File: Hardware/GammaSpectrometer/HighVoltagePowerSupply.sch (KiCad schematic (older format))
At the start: 59 parts, among them J1 power supply, J2 anode, J3 cathode, J4 Conn_01x07_Female, J5 RF_Shield_Two_Pieces, Q1 AOD2810, U1 MCP1416

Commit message: HV Power Supply and DataAcquisition will be placed on the same PCB. Due to EMI it mightl be needed to mount them on separate PCB, still they will share the same layout. This will decrease amount of needed PCBs and reduce costs.
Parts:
- J1: footprint HighVoltagePowerSupply:DG300-5.0-02P-12-00A(H) -> GammaSpectrometer:DG300-5.0-02P-12-00A(H)
- J5: footprint HighVoltagePowerSupply:3710.16 -> GammaSpectrometer:3710.16
- TR1: footprint HighVoltagePowerSupply:RM8 -> GammaSpectrometer:RM8; symbol HighVoltagePowerSupply:RM8 -> GammaSpectrometer:RM8

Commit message: Applied some remarks after second hw review (#104). Basically only removed voltage divider and replaced it by additional transformer winding.
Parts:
- removed C15: 1n, Capacitor_SMD:C_1206_3216Metric, symbol Device:C
- removed D3: 5V, Diode_SMD:D_SMA, symbol Device:D_Zener
- removed R10: 5k6, Resistor_SMD:R_MELF_MMB-0207, symbol Device:R
- removed R11, R12, R13, R14, R15, R7, R8, R9: 10M, Resistor_SMD:R_MELF_MMB-0207, symbol Device:R
- removed R16, R17: 47k, Resistor_SMD:R_MELF_MMB-0207, symbol Device:R
- added C15: 10u/12V, Capacitor_SMD:CP_Elec_10x10, symbol Device:CP
- added C17: 100n, Capacitor_SMD:C_1206_3216Metric, symbol Device:C
- added D3: D, symbol Device:D
- added L3: TBD, symbol Device:L_Core_Ferrite
- R5, R6: value 10M -> 6k8; footprint Resistor_SMD:R_MELF_MMB-0207 -> Resistor_SMD:R_1206_3216Metric
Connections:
- net labels removed: V_DIVIDER
- wire segments 178 -> 168
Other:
- moved on the sheet: C11, C12, C13, C14, C6, C8, D2, J2, J3, L2, R18, R4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

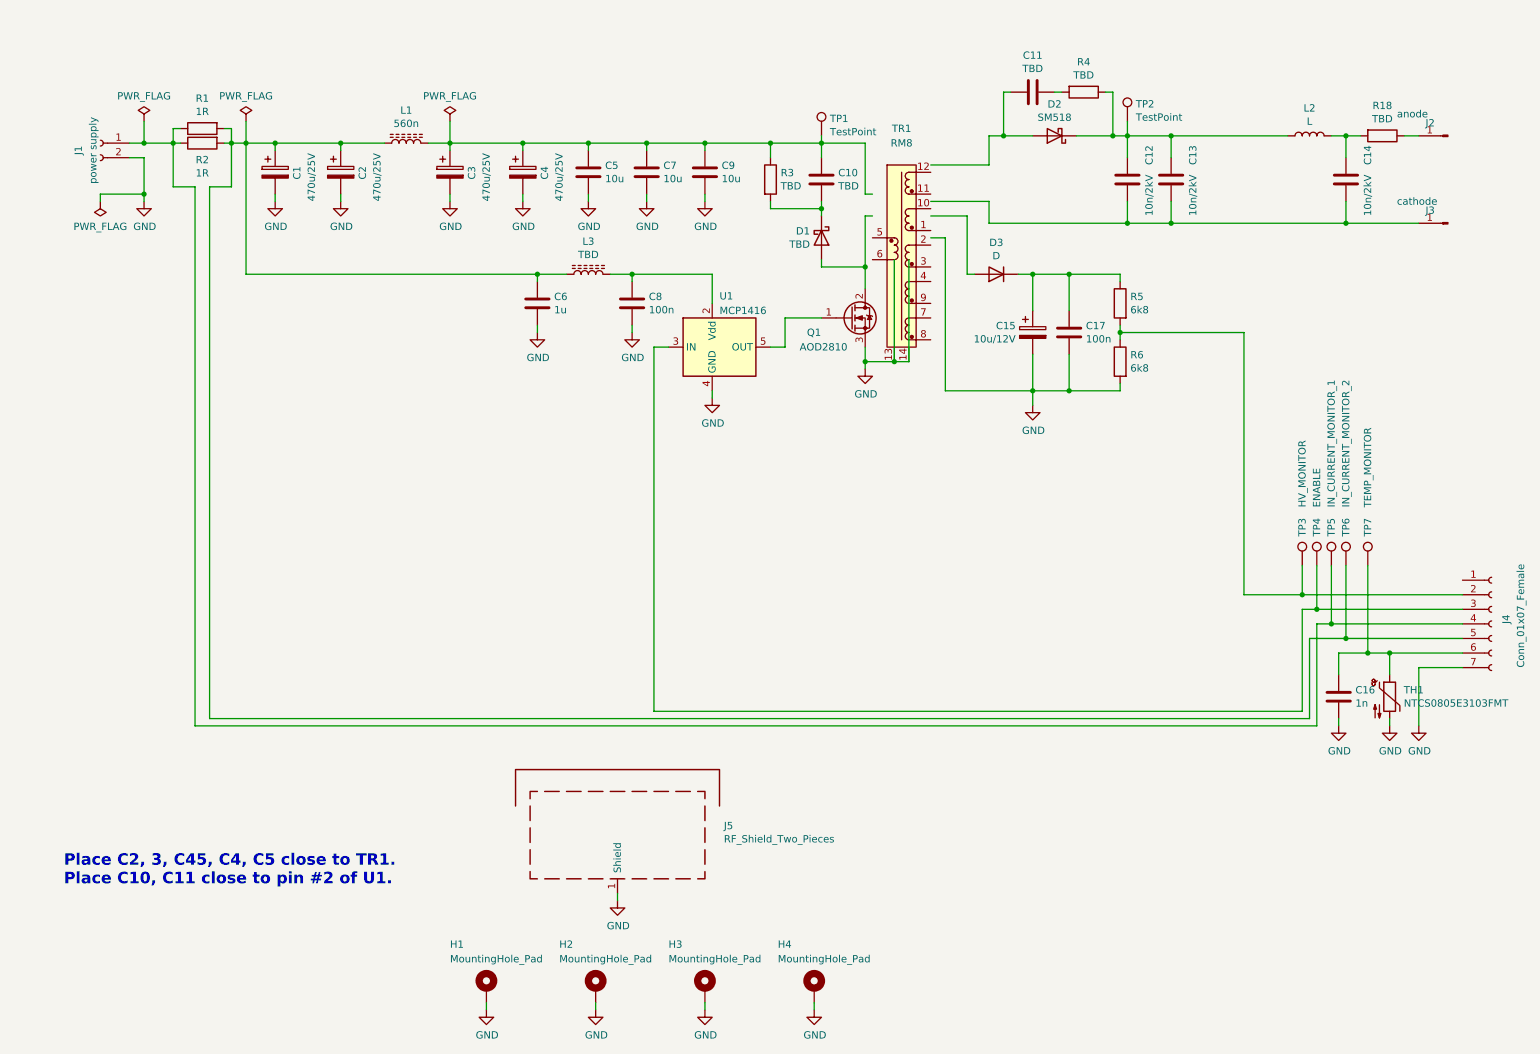
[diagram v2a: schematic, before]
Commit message: Output voltage is to high for a single diode, added multiple transformers windings and diode for each one, then connected outputs in series to obtain required voltage.
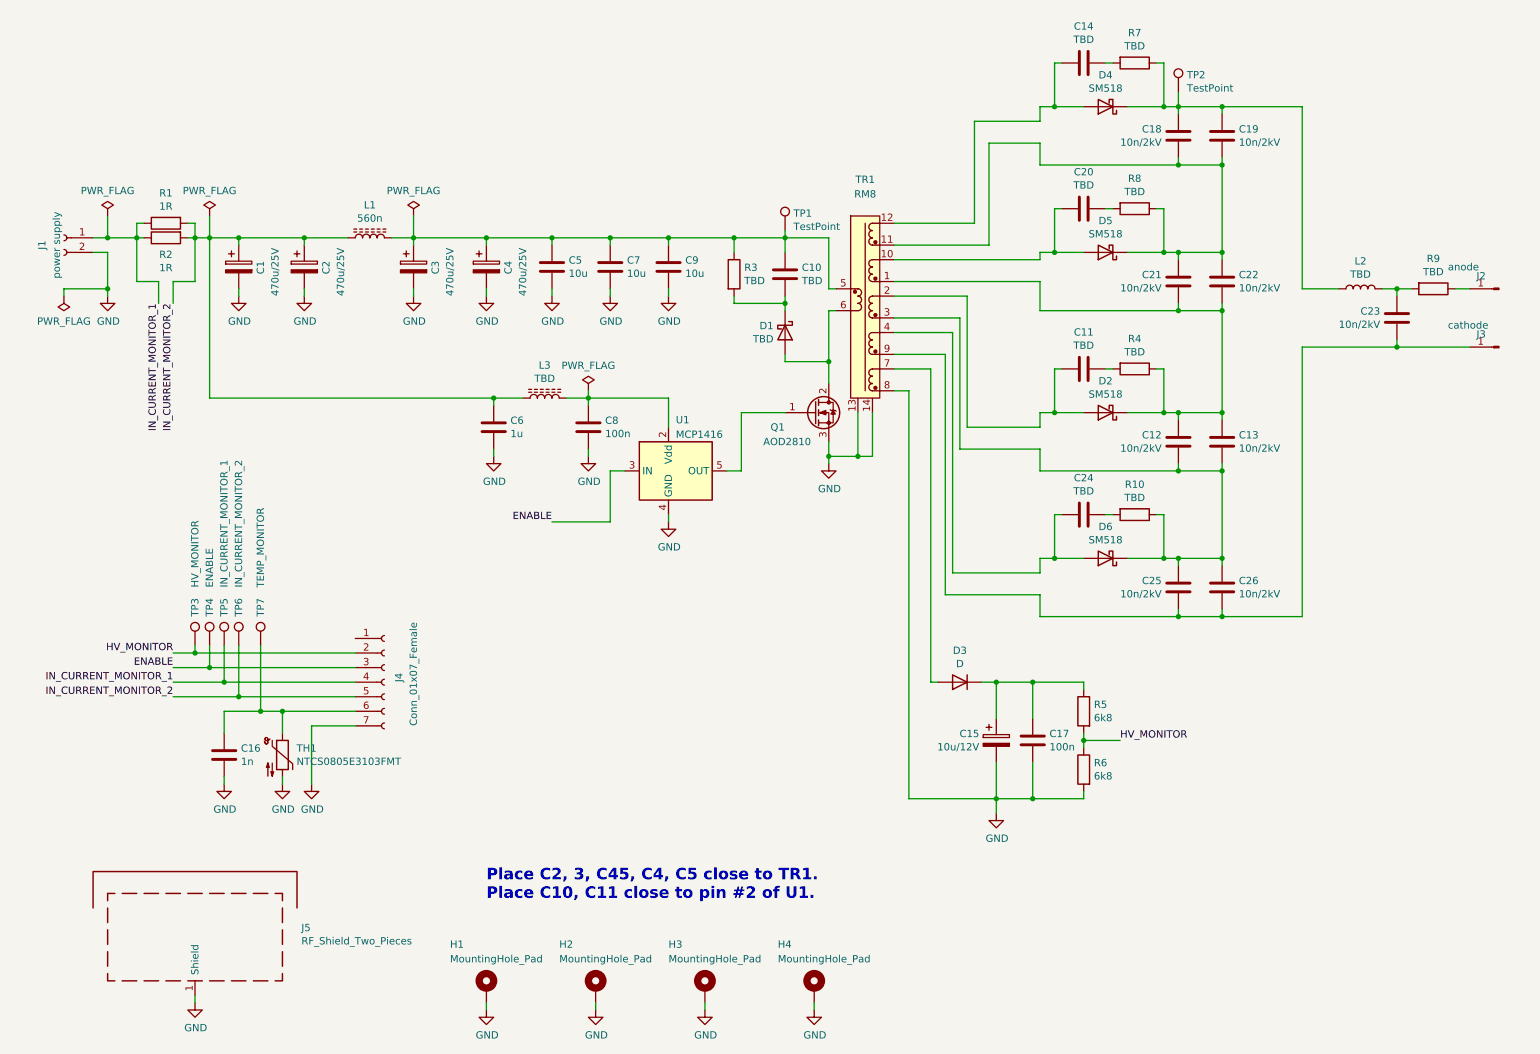
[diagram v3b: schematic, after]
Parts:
- removed R18: TBD, Resistor_THT:R_Axial_DIN0207_L6.3mm_D2.5mm_P10.16mm_Horizontal, symbol Device:R
- added C18, C19, C21, C22, C23, C25, C26: 10n/2kV, Capacitor_THT:C_Disc_D7.5mm_W5.0mm_P7.50mm, symbol Device:C
- added C20, C24: TBD, Capacitor_SMD:C_1206_3216Metric, symbol Device:C
- added D4, D5, D6: SM518, Diode_SMD:D_SMB, symbol Device:D_Schottky
- added R10, R7, R8: TBD, Resistor_SMD:R_MELF_MMB-0207, symbol Device:R
- added R9: TBD, Resistor_THT:R_Axial_DIN0207_L6.3mm_D2.5mm_P10.16mm_Horizontal, symbol Device:R
- C14: value 10n/2kV -> TBD; footprint Capacitor_THT:C_Disc_D7.5mm_W5.0mm_P7.50mm -> Capacitor_SMD:C_1206_3216Metric
- L2: value L -> TBD
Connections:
- net labels added: ENABLE, HV_MONITOR, IN_CURRENT_MONITOR_1, IN_CURRENT_MONITOR_2
- wire segments 168 -> 242
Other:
- moved on the sheet: C1, C10, C11, C12, C13, C15, C16, C17, C2, C3, C4, C5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

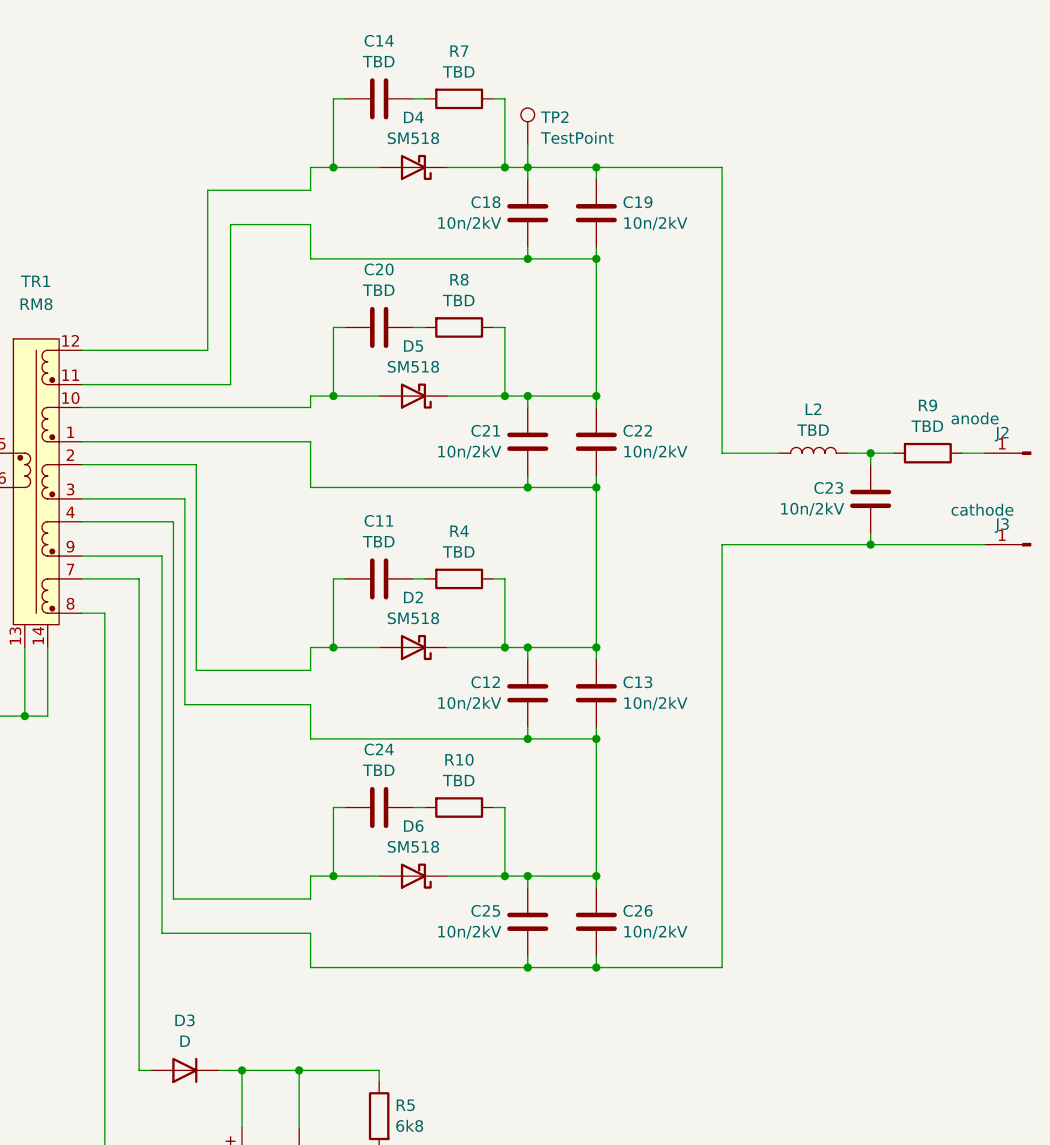
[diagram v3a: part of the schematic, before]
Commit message: Started creating simulation of paraller stabilizer for HV power supply. Rename simulation projects to fit theirs contents. Fix broken links.
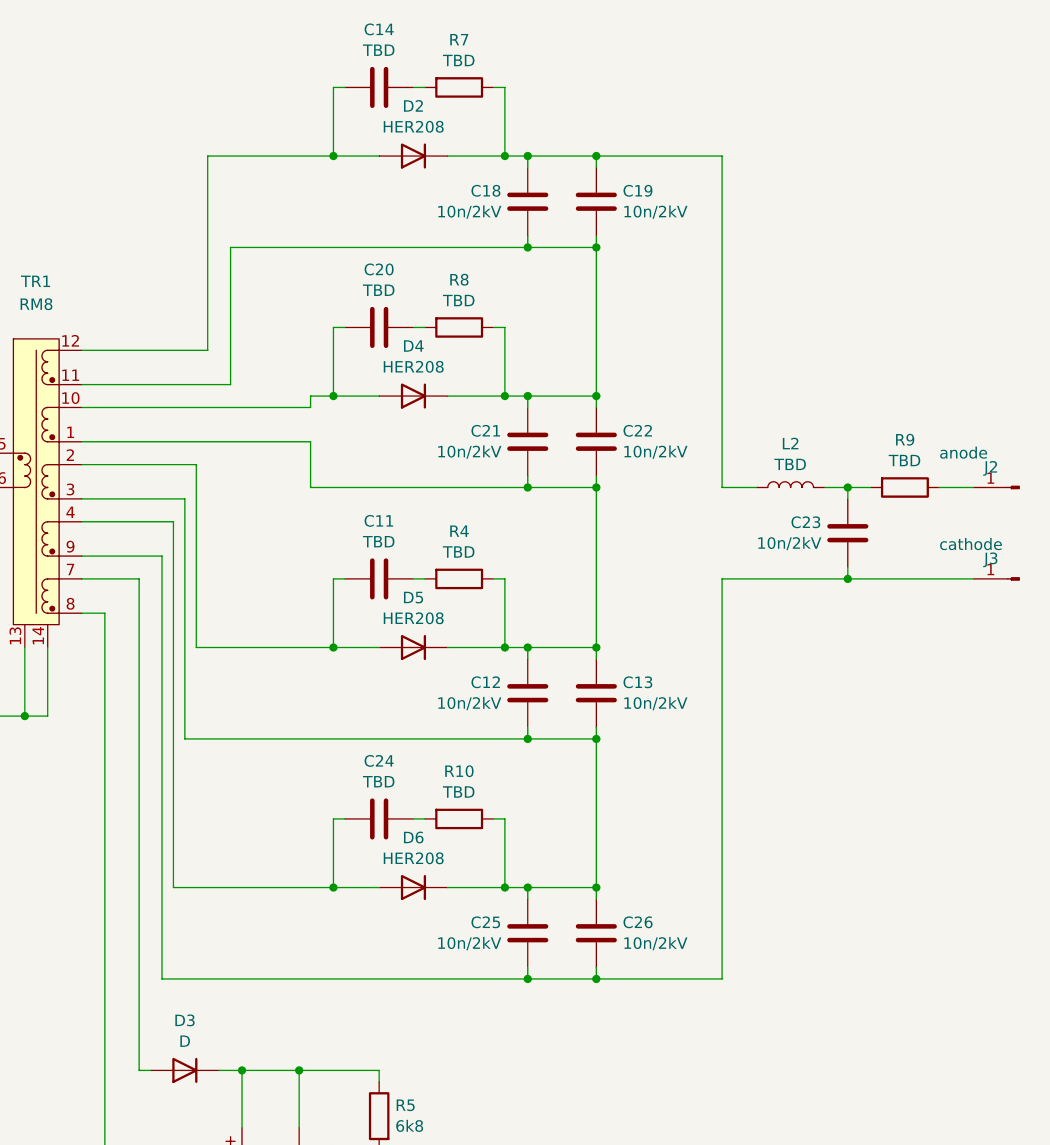
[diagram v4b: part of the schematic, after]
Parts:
- removed D2, D4, D5, D6: SM518, Diode_SMD:D_SMB, symbol Device:D_Schottky
- removed TP2: TestPoint, TestPoint:TestPoint_Pad_D1.5mm, symbol Connector:TestPoint
- added D2, D4, D5, D6: HER208, symbol Device:D
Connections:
- net at C12.2, C13.2, C21.1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: now also D5.1 (K)
- net at C11.1, TR1.2: now also D5.2 (A)
- net at C20.1, TR1.10: now also D4.2 (A)
- net at C18.1, C19.1, C21.2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: now also D4.1 (K)
- net at C14.1, TR1.12: now also D2.2 (A)
- net at C12.1, C13.1, C25.2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: now also D6.1 (K)
- net at C24.1, TR1.4: now also D6.2 (A)
- net at C18.2, C19.2, L2.1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: now also D2.1 (K)
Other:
- moved on the sheet: C14, C18, C19, C23, C24, C25, C26, J2, J3, L2, R10, R7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

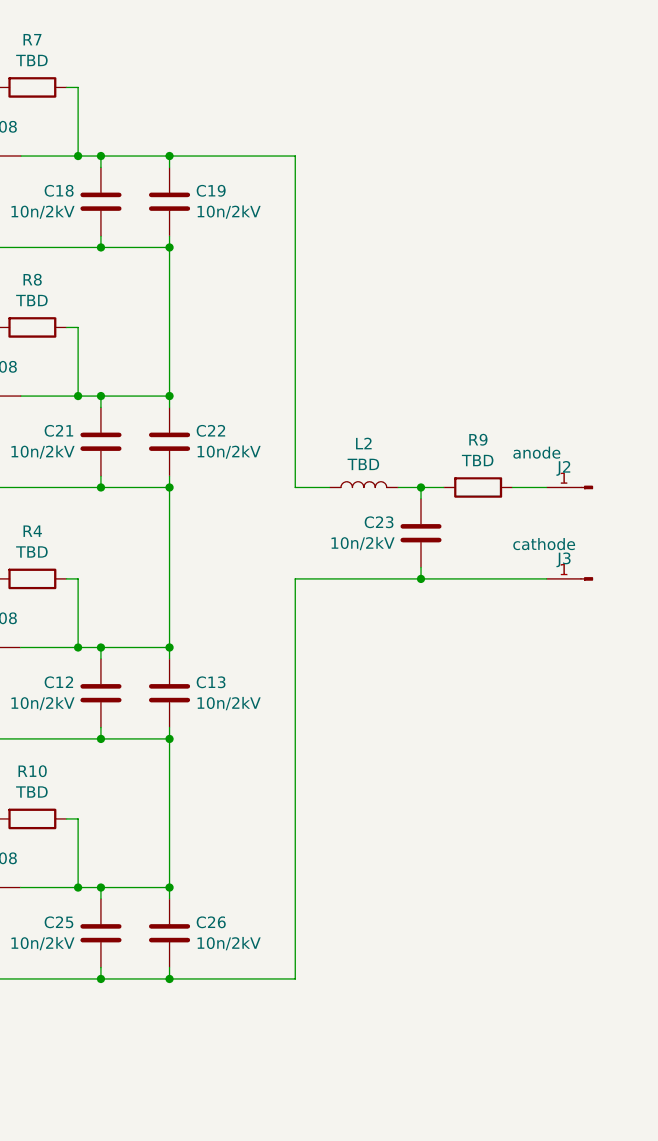
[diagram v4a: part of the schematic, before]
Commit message: Remove old version of simulation. In KiCad model added draft of HV stabilizer.
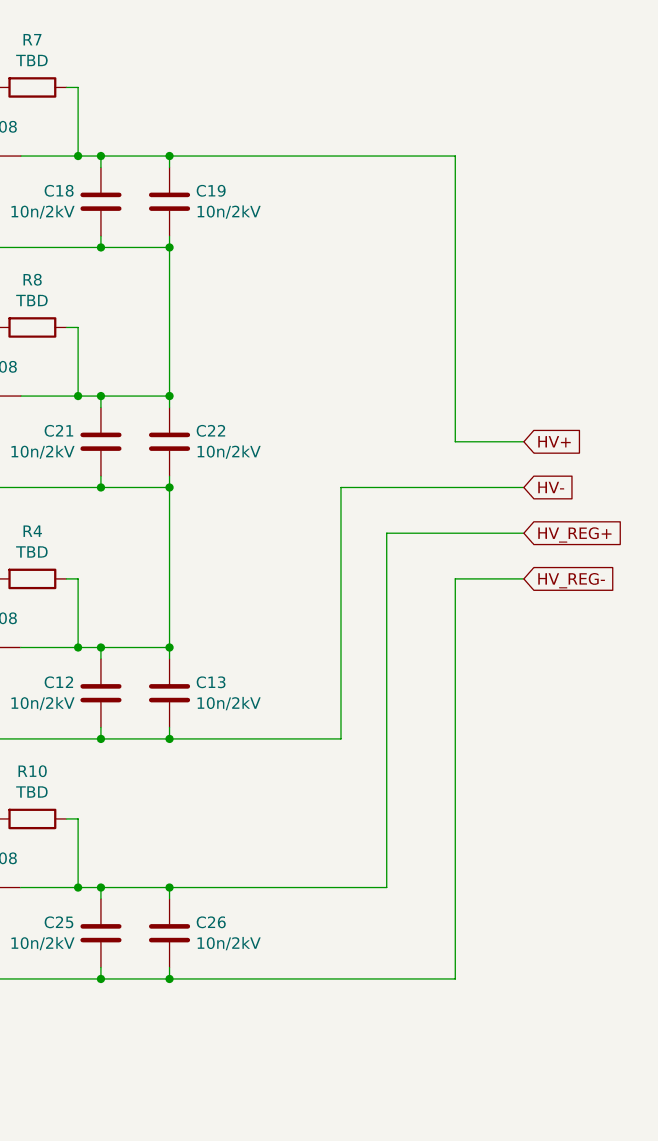
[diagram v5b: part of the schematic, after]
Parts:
- removed C23: 10n/2kV, Capacitor_THT:C_Disc_D7.5mm_W5.0mm_P7.50mm, symbol Device:C
- removed J2: anode, TestPoint:TestPoint_Loop_D2.54mm_Drill1.5mm_Beaded, symbol Connector:Conn_01x01_Male
- removed J3: cathode, TestPoint:TestPoint_Loop_D2.54mm_Drill1.5mm_Beaded, symbol Connector:Conn_01x01_Male
- removed L2: TBD, Inductor_SMD:L_10.4x10.4_H4.8, symbol Device:L
- removed R9: TBD, Resistor_THT:R_Axial_DIN0207_L6.3mm_D2.5mm_P10.16mm_Horizontal, symbol Device:R
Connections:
- net HV_REG+: now reaches C25.2, C26.2, D6.1 (K), R10.1
- net HV_REG+: no longer C12.1, C13.1, TR1.3
- net HV_REG-: now reaches C25.1, C26.1, TR1.9
- net HV+: now reaches C18.2, C19.2, D2.1 (K), R7.1
- new net HV-: C12.1, C13.1, TR1.3
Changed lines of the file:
@@
 $Descr A4 11693 8268
 encoding utf-8
-Sheet 2 3
+Sheet 2 4
 Title ""
 Date ""
@@
 $EndComp
 $Comp
-L Connector:Conn_01x01_Male J2
-U 1 1 5FE347F4
-P 10650 2750
-F 0 "J2" H 10804 2662 50  0000 R CNN
-F 1 "anode" H 11000 2600 50  0000 R CNN
-F 2 "TestPoint:TestPoint_Loop_D2.54mm_Drill1.5mm_Beaded" H 10650 2750 50  0001 C CNN
-F 3 "~" H 10650 2750 50  0001 C CNN
-	1    10650 2750
-	-1   0    0    1
-$EndComp
-$Comp
-L Connector:Conn_01x01_Male J3
-U 1 1 5FE347FA
-P 10650 3150
-F 0 "J3" H 10804 3062 50  0000 R CNN
-F 1 "cathode" H 11000 3000 50  0000 R CNN
-F 2 "TestPoint:TestPoint_Loop_D2.54mm_Drill1.5mm_Beaded" H 10650 3150 50  0001 C CNN
-F 3 "~" H 10650 3150 50  0001 C CNN
-	1    10650 3150
-	-1   0    0    1
-$EndComp
-$Comp
 L Device:C C?
 U 1 1 5FE34806
@@
 Wire Wire Line
 	8400 1300 8500 1300
-$Comp
-L Device:R R?
-U 1 1 5FE34829
-P 10150 2750
-AR Path="/5EDA53F3/5FE34829" Ref="R?"  Part="1"
-AR Path="/5EDA5628/5FE34829" Ref="R?"  Part="1"
-AR Path="/5FE34829" Ref="R?"  Part="1"
-AR Path="/5FBBA154/5FE34829" Ref="R9"  Part="1"
-F 0 "R9" V 9943 2750 50  0000 C CNN
-F 1 "TBD" V 10034 2750 50  0000 C CNN
-F 2 "Resistor_THT:R_Axial_DIN0207_L6.3mm_D2.5mm_P10.16mm_Horizontal" V 10080 2750 50  0001 C CNN
-F 3 "~" H 10150 2750 50  0001 C CNN
-	1    10150 2750
-	0    1    1    0
-$EndComp
-Wire Wire Line
-	10300 2750 10450 2750
 Wire Wire Line
 	8500 1700 8800 1700
-$Comp
-L Device:L L2
-U 1 1 5FE34831
-P 9650 2750
-F 0 "L2" V 9840 2750 50  0000 C CNN
-F 1 "TBD" V 9749 2750 50  0000 C CNN
-F 2 "Inductor_SMD:L_10.4x10.4_H4.8" H 9650 2750 50  0001 C CNN
-F 3 "https://www.tme.eu/Document/18f8a623126e52c1b46a51bde1bd900b/SDR1006.pdf" H 9650 2750 50  0001 C CNN
-	1    9650 2750
-	0    -1   -1   0
-$EndComp
 Wire Wire Line
 	8800 1350 8800 1300
@@
 $EndComp
 Wire Wire Line
-	9900 2800 9900 2750
-Wire Wire Line
-	9900 3100 9900 3150
-$Comp
-L Device:C C?
-U 1 1 5FE3484A
-P 9900 2950
-AR Path="/5EDA53F3/5FE3484A" Ref="C?"  Part="1"
-AR Path="/5EDA5628/5FE3484A" Ref="C?"  Part="1"
-AR Path="/5FE3484A" Ref="C?"  Part="1"
-AR Path="/5FBBA154/5FE3484A" Ref="C23"  Part="1"
-F 0 "C23" H 10015 2904 50  0000 L CNN
-F 1 "10n/2kV" H 10015 2995 50  0000 L CNN
-F 2 "Capacitor_THT:C_Disc_D7.5mm_W5.0mm_P7.50mm" H 9938 2800 50  0001 C CNN
-F 3 "~" H 9900 2950 50  0001 C CNN
-	1    9900 2950
-	-1   0    0    1
-$EndComp
-Wire Wire Line
-	9800 2750 9900 2750
-Connection ~ 9900 2750
-Wire Wire Line
-	9900 2750 10000 2750
-Wire Wire Line
-	9900 3150 10450 3150
-Wire Wire Line
-	8800 1300 9350 1300
+	8800 1300 10050 1300
 $Comp
 L Device:C C?
@@
 Connection ~ 8800 3450
 Wire Wire Line
-	8800 3850 8800 4500
-Connection ~ 8800 3850
-Connection ~ 8800 4500
-Wire Wire Line
-	9350 1300 9350 2750
-Wire Wire Line
-	9350 2750 9500 2750
-Wire Wire Line
-	8800 4900 9350 4900
-Wire Wire Line
-	9350 4900 9350 3150
-Wire Wire Line
-	9350 3150 9900 3150
+	10050 1300 10050 2550
+Wire Wire Line
+	8800 4900 10050 4900
 Connection ~ 8800 4900
-Connection ~ 9900 3150
 $Comp
 L power:PWR_FLAG #FLG05
@@
 Wire Wire Line
 	7050 3450 7650 3450
+Wire Wire Line
+	10050 4900 10050 3150
+Wire Wire Line
+	8800 4500 9750 4500
+Wire Wire Line
+	9750 4500 9750 2950
+Wire Wire Line
+	9750 2950 10350 2950
+Connection ~ 8800 4500
+Wire Wire Line
+	10050 2550 10350 2550
+Wire Wire Line
+	10050 3150 10350 3150
+Text GLabel 10350 2550 2    50   Input ~ 0
+HV+
+Text GLabel 10350 3150 2    50   Input ~ 0
+HV_REG-
+Text GLabel 10350 2950 2    50   Input ~ 0
+HV_REG+
+Wire Wire Line
+	8800 3850 9550 3850
+Wire Wire Line
+	9550 3850 9550 2750
+Wire Wire Line
+	9550 2750 10350 2750
+Connection ~ 8800 3850
+Text GLabel 10350 2750 2    50   Input ~ 0
+HV-
 $EndSCHEMATC
